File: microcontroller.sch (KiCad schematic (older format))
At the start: 18 parts, among them J6 I2C, SW1 SW_Push, U3 ESP32-DEVKITC-32D

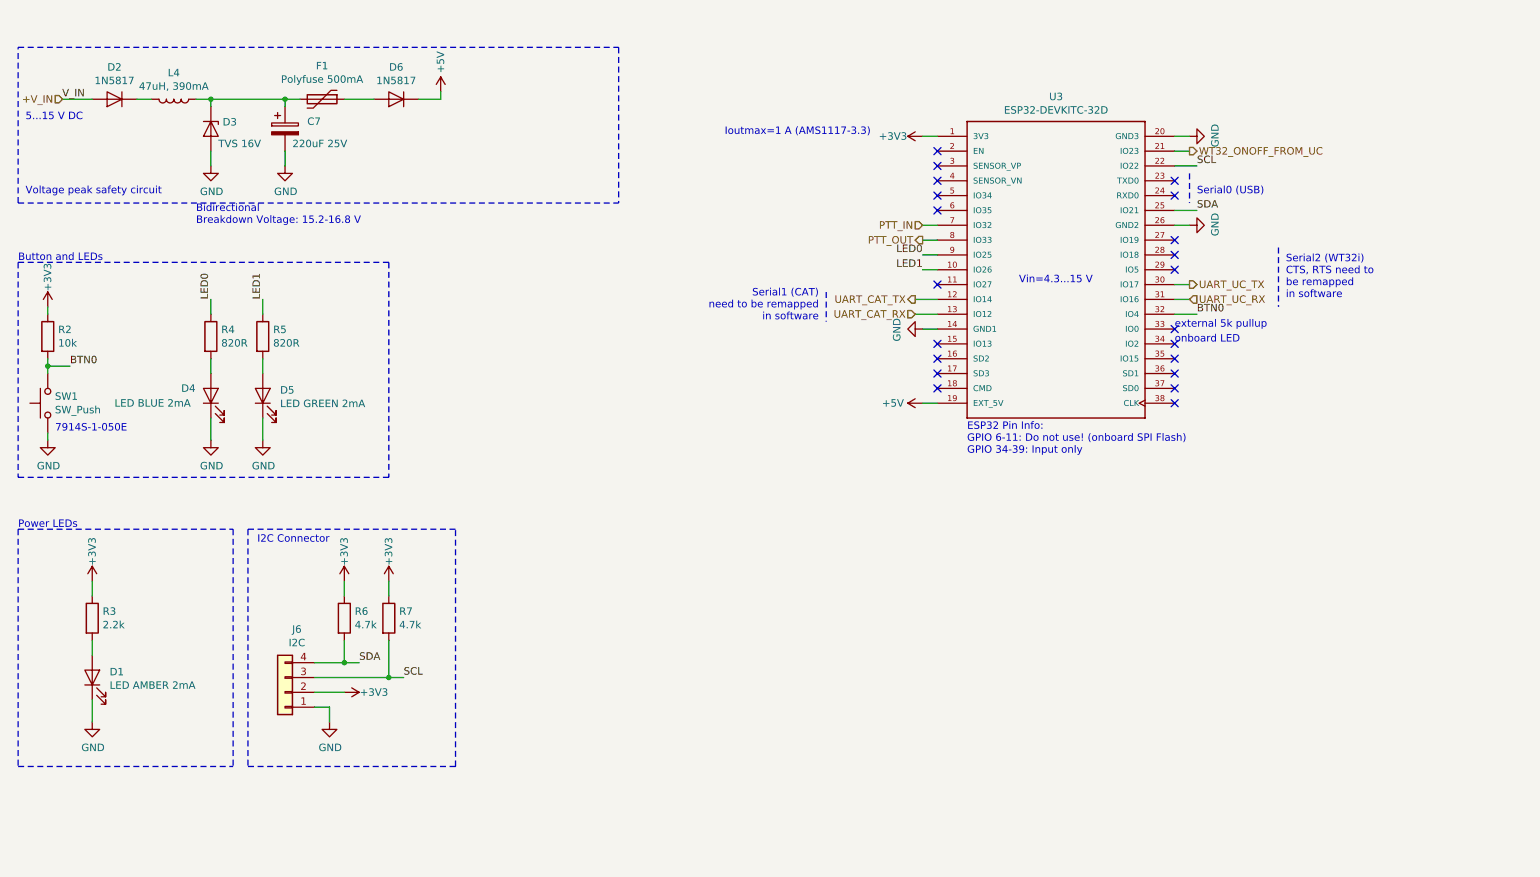
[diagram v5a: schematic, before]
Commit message: [#1] Continued PCB
* Moved button pin for better tracability
* Added all missing traces
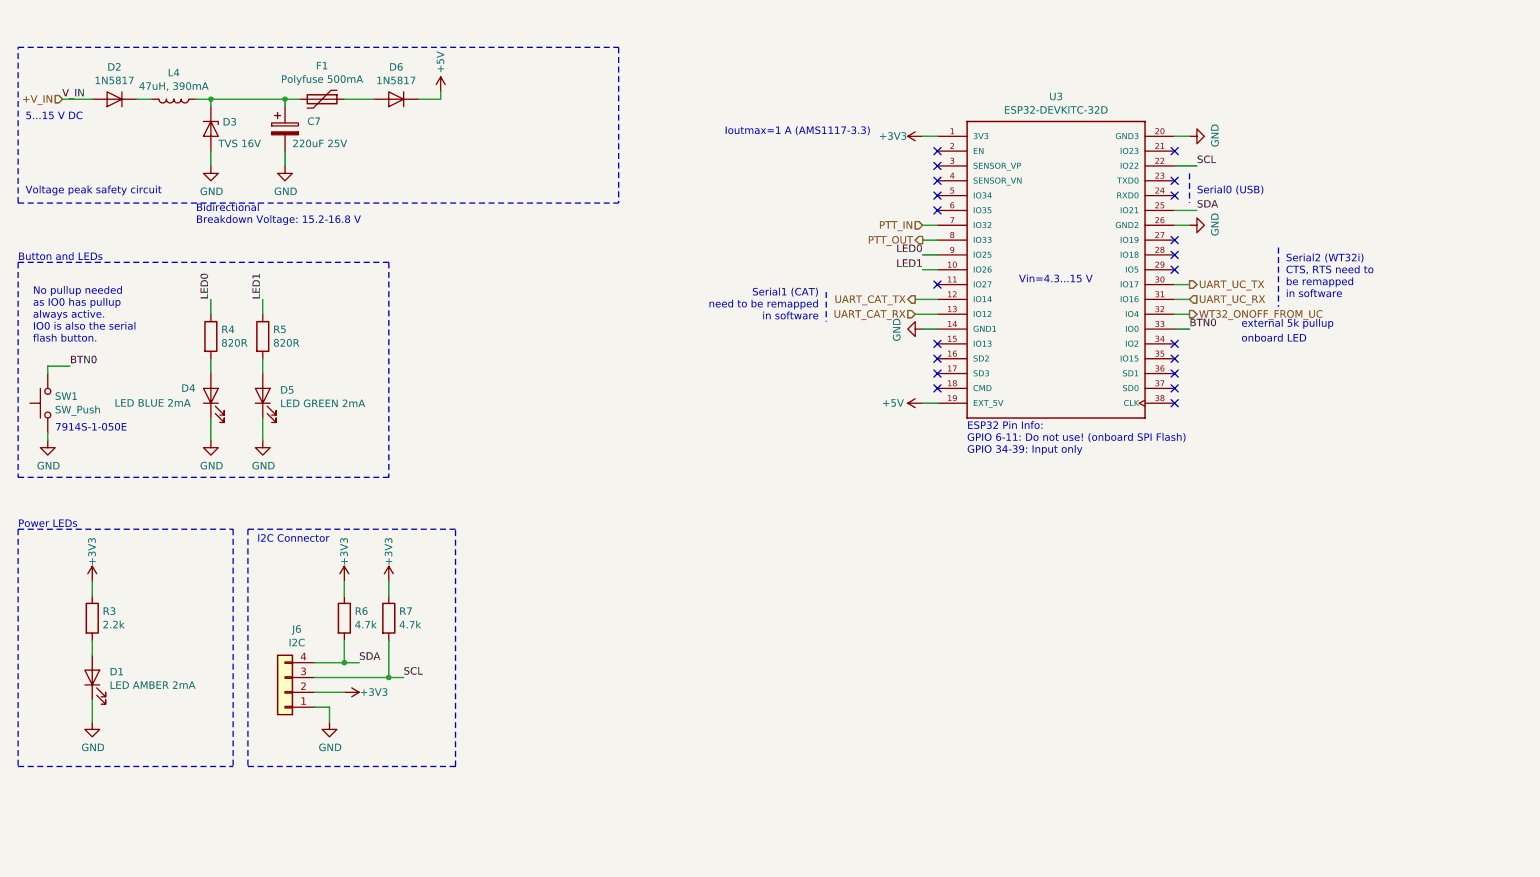
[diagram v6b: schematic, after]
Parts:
- removed R2: 10k, Resistor_SMD:R_0805_2012Metric_Pad1.15x1.40mm_HandSolder, symbol Device:R
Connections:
- net BTN0: now also U3.33 (IO0); no longer U3.32 (IO4)
- net WT32_ONOFF_FROM_UC: now also U3.32 (IO4); no longer U3.21 (IO23)
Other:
- note added: "No pullup needed\nas IO0 has pullup\nalways active.\nIO0 is also the serial \nflash button."
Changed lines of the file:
@@
 Wire Wire Line
 	900  2850 1050 2850
-Wire Wire Line
-	900  2850 900  2800
-$Comp
-L Device:R R?
-U 1 1 5C1540CA
-P 900 2650
-AR Path="/5C1540CA" Ref="R?"  Part="1"
-AR Path="/5C10B93A/5C1540CA" Ref="R2"  Part="1"
-F 0 "R2" H 970 2696 50  0000 L CNN
-F 1 "10k" H 970 2605 50  0000 L CNN
-F 2 "Resistor_SMD:R_0805_2012Metric_Pad1.15x1.40mm_HandSolder" V 830 2650 50  0001 C CNN
-F 3 "~" H 900 2650 50  0001 C CNN
-F 4 "603-RC0805FR-0710KL" H -2750 -2500 50  0001 C CNN "Mouser Best.Nr."
-	1    900  2650
-	1    0    0    -1
-$EndComp
-Wire Wire Line
-	900  2450 900  2500
 Text Label 1050 2850 0    50   ~ 0
 BTN0
@@
 Text Label 6800 2200 2    50   ~ 0
 LED1
-Text HLabel 8600 1400 2    50   Output ~ 0
+Text HLabel 8600 2500 2    50   Output ~ 0
 WT32_ONOFF_FROM_UC
-Text Label 8650 2500 0    50   ~ 0
+Text Label 8600 2600 0    50   ~ 0
 BTN0
 Wire Wire Line
@@
 Text HLabel 6800 1900 0    50   Input ~ 0
 PTT_IN
-$Comp
-L power:+3V3 #PWR?
-U 1 1 5C7D8BC0
-P 900 2450
-AR Path="/5C7D8BC0" Ref="#PWR?"  Part="1"
-AR Path="/5C10B93A/5C7D8BC0" Ref="#PWR021"  Part="1"
-F 0 "#PWR021" H 900 2300 50  0001 C CNN
-F 1 "+3V3" V 900 2650 50  0000 C CNN
-F 2 "" H 900 2450 50  0001 C CNN
-F 3 "" H 900 2450 50  0001 C CNN
-	1    900  2450
-	1    0    0    -1
-$EndComp
 Wire Notes Line
 	700  3950 2150 3950
@@
 Text HLabel 6800 2000 0    50   Output ~ 0
 PTT_OUT
-Connection ~ 900  2850
 Text Notes 950  3300 0    50   ~ 0
 7914S-1-050E
-Wire Wire Line
-	8500 2500 8650 2500
 Wire Wire Line
 	2000 2800 2000 2900
@@
 Wire Notes Line
 	6150 2350 6150 2550
-Wire Wire Line
-	8500 1400 8600 1400
 Text Label 8650 1800 0    50   ~ 0
 SDA
@@
 Wire Wire Line
 	6800 2600 6900 2600
-NoConn ~ 8500 2700
-Text Notes 8500 2700 0    50   ~ 0
+Text Notes 8950 2700 0    50   ~ 0
 onboard LED
-NoConn ~ 8500 2600
-Text Notes 8500 2600 0    50   ~ 0
+Text Notes 8950 2600 0    50   ~ 0
 external 5k pullup
 Wire Notes Line
@@
 NoConn ~ 6900 2300
 NoConn ~ 8500 2100
+Wire Wire Line
+	8500 2500 8600 2500
+NoConn ~ 8500 1400
+NoConn ~ 8500 2700
 NoConn ~ 8500 2200
+Wire Wire Line
+	8500 2600 8600 2600
+Text Notes 800  2700 0    50   ~ 0
+No pullup needed\nas IO0 has pullup\nalways active.\nIO0 is also the serial \nflash button.
 $EndSCHEMATC

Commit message: [#2] Update Schematic with new Footprint for ESP32 Board
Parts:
- U3: footprint ESP32-DEVKITC-32D:MODULE_ESP32-DEVKITC-32D -> nodemcu_esp-32s:ESP-32_NodeMCU
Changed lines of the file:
@@
 EESchema Schematic File Version 4
 LIBS:bt-trx-dev-board-cache
-EELAYER 29 0
+EELAYER 26 0
 EELAYER END
 $Descr A4 11693 8268
@@
 F 0 "U3" H 7700 3367 50  0000 C CNN
 F 1 "ESP32-DEVKITC-32D" H 7700 3276 50  0000 C CNN
-F 2 "ESP32-DEVKITC-32D:MODULE_ESP32-DEVKITC-32D" H 7700 2200 50  0001 L BNN
+F 2 "nodemcu_esp-32s:ESP-32_NodeMCU" H 7700 2200 50  0001 L BNN
 F 3 "None" H 7700 2200 50  0001 L BNN
 F 4 "Espressif Systems" H 7700 2200 50  0001 L BNN "Field4"
